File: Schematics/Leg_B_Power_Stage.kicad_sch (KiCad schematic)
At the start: 0 parts

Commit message: [LEG A WIP]
- moved circuits in Leg A HS and LS
- Completed 90% of HS and LS for LEG A
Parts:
- added Q5, Q6: C3M0025065K, SiC_Inverter:C3M0025065K, symbol SiC_Inverter:C3M0025065K
- added U3, U4: UCC21710QDWRQ1, SiC_Inverter:UCC21710QDWRQ1, symbol SiC_Inverter:UCC21710QDWRQ1

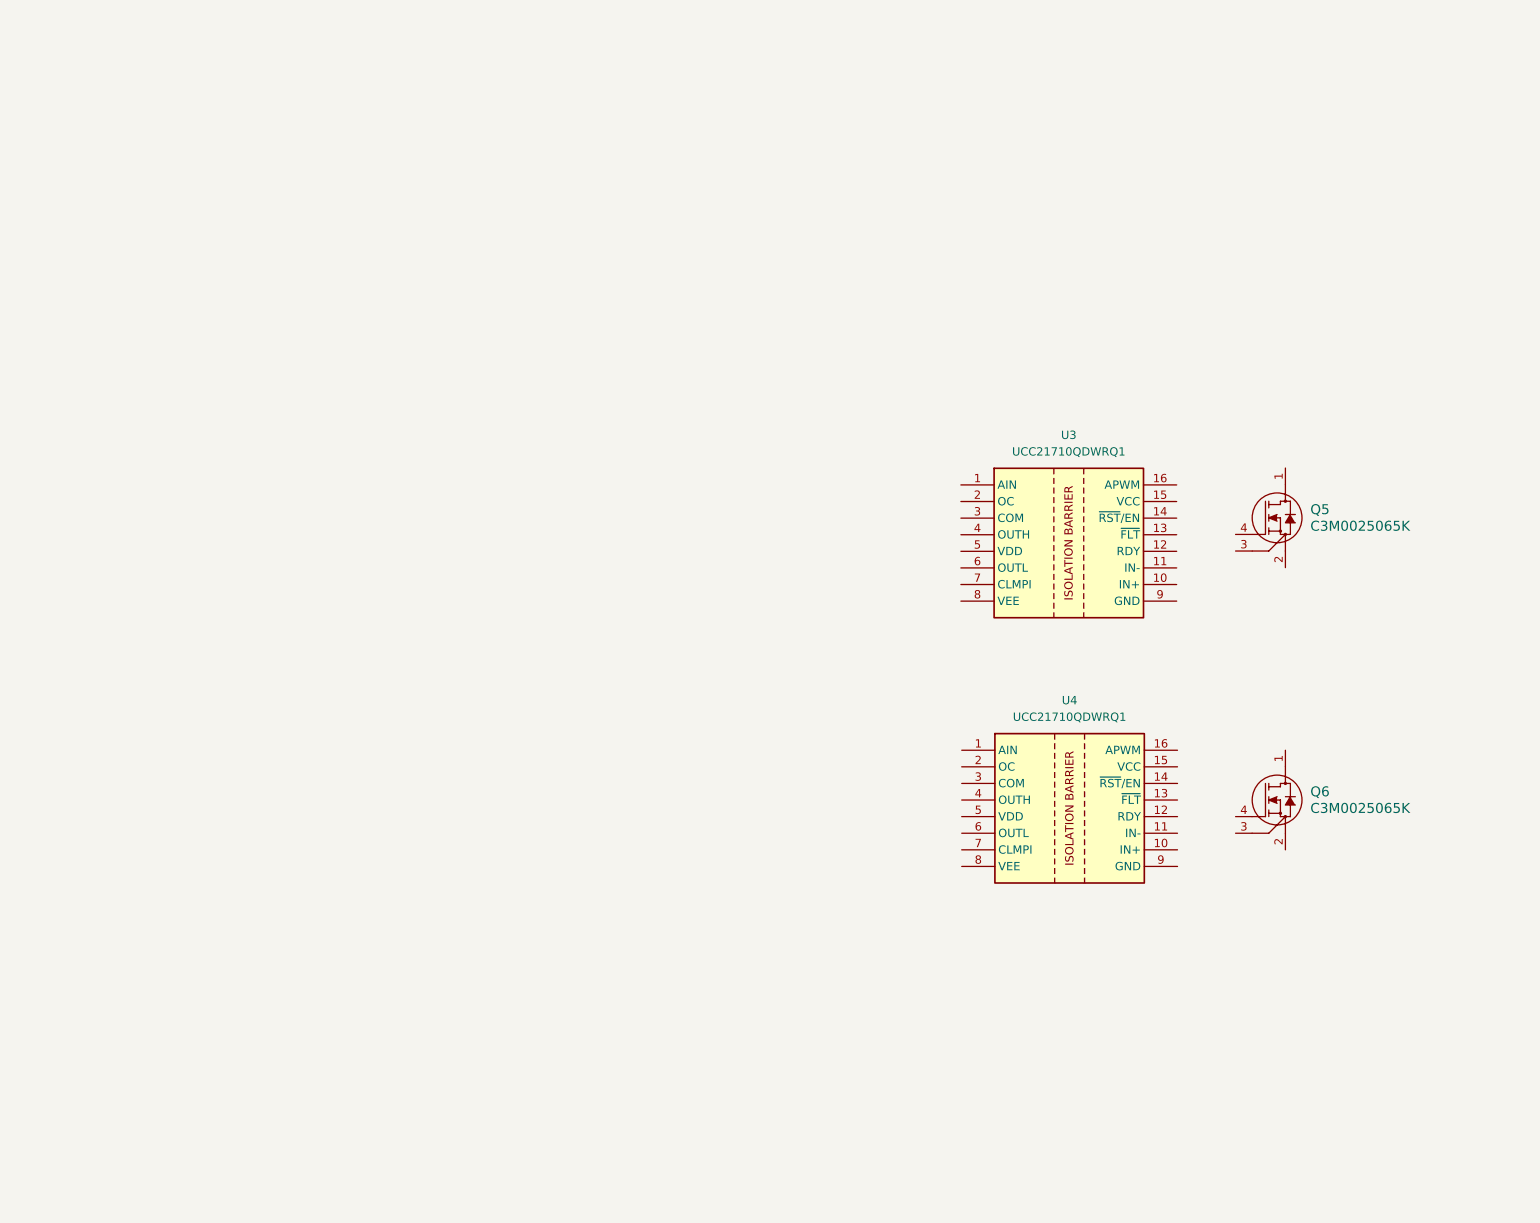
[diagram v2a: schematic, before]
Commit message: Copy past Leg A onto Leg B, Changed hames on both High/Low side to match Leg B
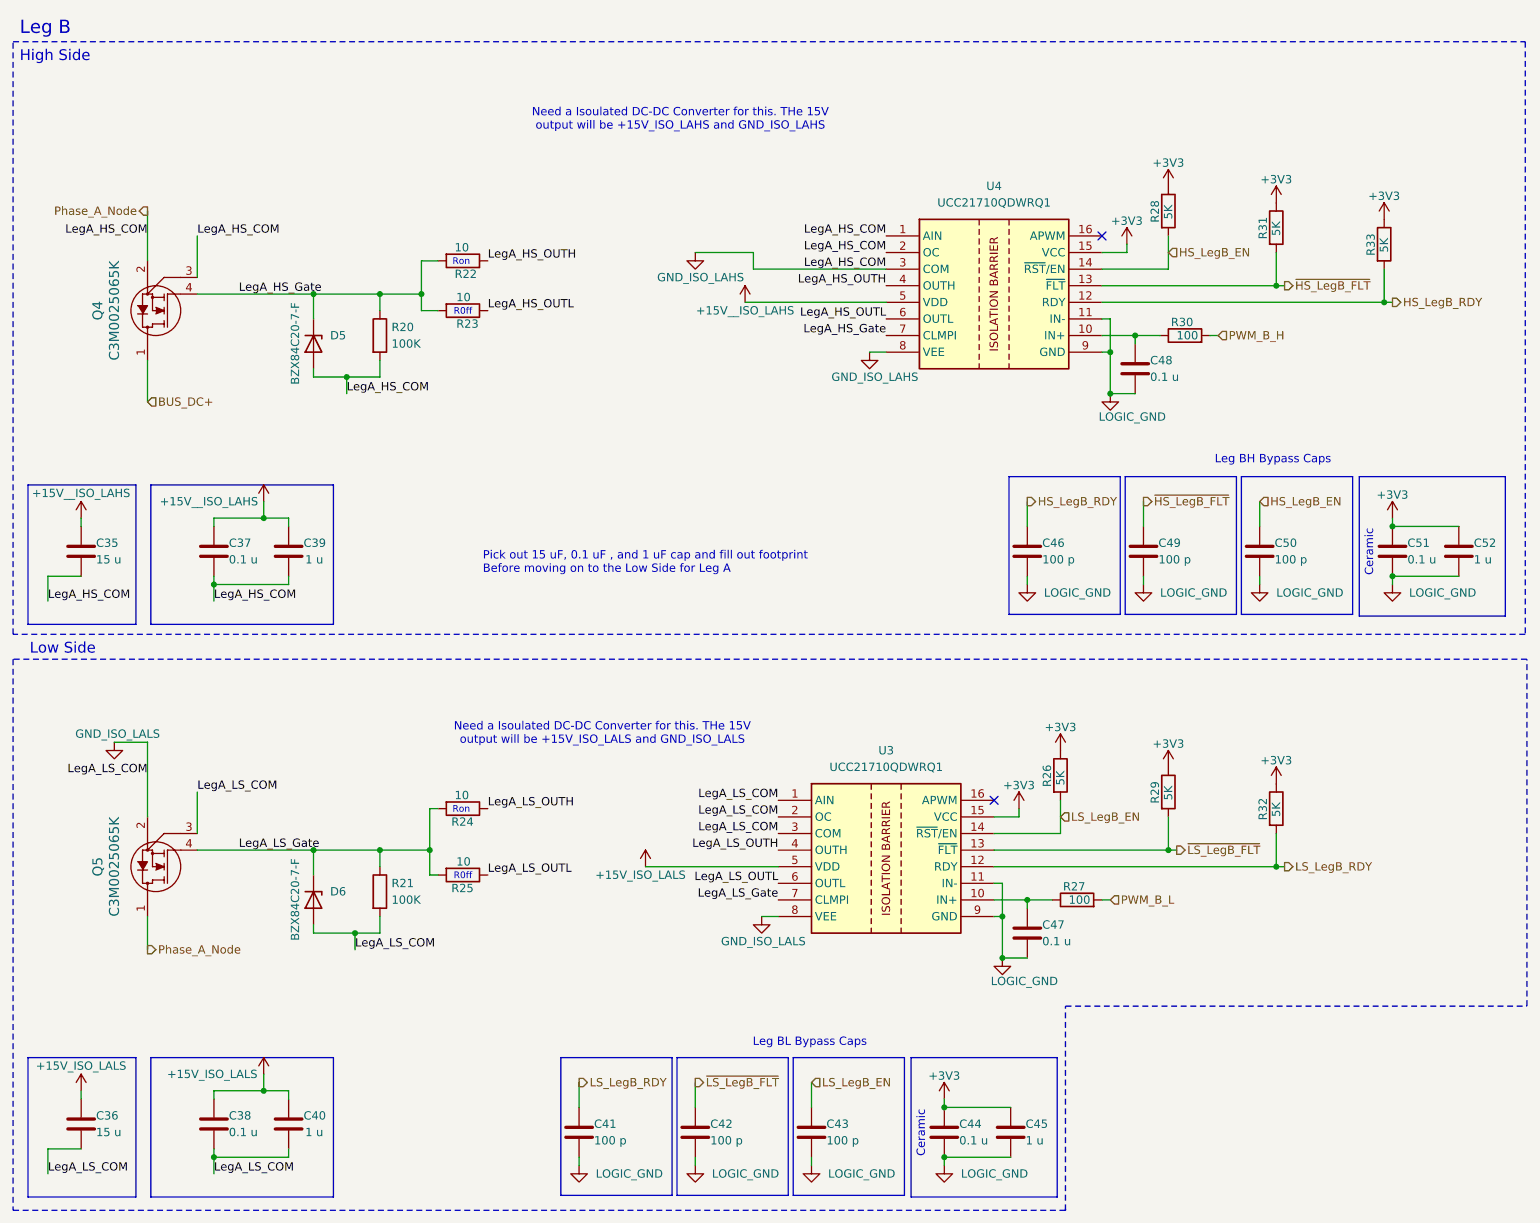
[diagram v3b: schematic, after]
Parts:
- removed Q6: C3M0025065K, SiC_Inverter:C3M0025065K, symbol SiC_Inverter:C3M0025065K
- added C35, C36: 15 u, symbol Device:C
- added C37, C38, C44, C47, C48, C51: 0.1 u, symbol Device:C
- added C39, C40, C45, C52: 1 u, symbol Device:C
- added C41, C42, C43, C46, C49, C50: 100 p, symbol Device:C
- added D5, D6: BZX84C20-7-F, Package_TO_SOT_SMD:SOT-23-3, symbol SiC_Inverter:BZX84C20-7-F
- added Q4: C3M0025065K, SiC_Inverter:C3M0025065K, symbol SiC_Inverter:C3M0025065K
- added R20, R21: 100K, Resistor_SMD:R_1206_3216Metric_Pad1.30x1.75mm_HandSolder, symbol Device:R
- added R22, R23, R24, R25: 10, Resistor_SMD:R_1206_3216Metric_Pad1.30x1.75mm_HandSolder, symbol Device:R
- added R26, R28, R29, R31, R32, R33: 5K, Resistor_SMD:R_1206_3216Metric_Pad1.30x1.75mm_HandSolder, symbol Device:R
- added R27, R30: 100, Resistor_SMD:R_1206_3216Metric_Pad1.30x1.75mm_HandSolder, symbol Device:R
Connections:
- net GND_ISO_LAHS: now reaches U4.1 (AIN)
- net GND_ISO_LAHS: now also Q5.1, U4.2 (OC), U4.3 (COM), U4.8 (VEE), C35.2, C37.2, C39.2, D5.2 (A), Q4.2, Q4.3, R20.2
- net at U4.10 (IN+): now also C48.1, R30.1
- net LOGIC_GND: now reaches U4.11 (IN-)
- net LOGIC_GND: now also U3.11 (IN-), U3.9 (GND), U4.9 (GND), C41.2, C42.2, C43.2, C44.2, C45.2, C46.2, C47.2, C48.2, C49.2, C50.2, C51.2, C52.2
- net HS_LegB_RDY: now reaches U4.12 (RDY)
- net HS_LegB_RDY: now also C46.1, R33.2
- net ~{HS_LegB_FLT}: now reaches U4.13 (~{FLT})
- net ~{HS_LegB_FLT}: now also C49.1, R31.2
- net HS_LegB_EN: now reaches U4.14 (~{RST}/EN)
- net HS_LegB_EN: now also C50.1, R28.2
- net +3V3: now reaches U4.15 (VCC)
- net +3V3: now also U3.15 (VCC), C44.1, C45.1, C51.1, C52.1, R26.1, R28.1, R29.1, R31.1, R32.1, R33.1
- net LegA_HS_OUTH: now reaches U4.4 (OUTH)
- net LegA_HS_OUTH: now also R22.1
- net +15V__ISO_LAHS: now reaches U4.5 (VDD)
- net +15V__ISO_LAHS: now also C35.1, C37.1, C39.1
- net LegA_HS_OUTL: now reaches U4.6 (OUTL)
- net LegA_HS_OUTL: now also R23.1
- net LegA_HS_Gate: now reaches U4.7 (CLMPI)
- net LegA_HS_Gate: now also D5.1 (K), Q4.4, R20.1, R22.2, R23.2
- net GND_ISO_LALS: now reaches U3.1 (AIN)
- net GND_ISO_LALS: now also Q5.2, Q5.3, U3.2 (OC), U3.3 (COM), U3.8 (VEE), C36.2, C38.2, C40.2, D6.2 (A), R21.2
- net at U3.10 (IN+): now also C47.1, R27.1
- net LS_LegB_RDY: now reaches U3.12 (RDY)
- net LS_LegB_RDY: now also C41.1, R32.2
- net ~{LS_LegB_FLT}: now reaches U3.13 (~{FLT})
- net ~{LS_LegB_FLT}: now also C42.1, R29.2
- net LS_LegB_EN: now reaches U3.14 (~{RST}/EN)
- net LS_LegB_EN: now also C43.1, R26.2
- net LegA_LS_OUTH: now reaches U3.4 (OUTH)
- net LegA_LS_OUTH: now also R24.1
- net +15V_ISO_LALS: now reaches U3.5 (VDD)
- net +15V_ISO_LALS: now also C36.1, C38.1, C40.1
- net LegA_LS_OUTL: now reaches U3.6 (OUTL)
- net LegA_LS_OUTL: now also R25.1
- net LegA_LS_Gate: now reaches U3.7 (CLMPI)
- net LegA_LS_Gate: now also Q5.4, D6.1 (K), R21.1, R24.2, R25.2
- new net BUS_DC+: Q4.1
- new net PWM_B_H: R30.2
- new net PWM_B_L: R27.2
- no-connect marks 0 -> 2
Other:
- note added: "Ceramic"
- note added: "High Side"
- note added: "Leg B"
- note added: "Leg BH Bypass Caps"
- note added: "Leg BL Bypass Caps"
- note added: "Low Side"
- note added: "Need a Isoulated DC-DC Converter for this. THe 15V output will be +15V_ISO_LAHS and GND_ISO_LAHS"
- note added: "Need a Isoulated DC-DC Converter for this. THe 15V output will be +15V_ISO_LALS and GND_ISO_LALS"
- note added: "Pick out 15 uF, 0.1 uF , and 1 uF cap and fill out footprint Before moving on to the Low Side for Leg A"
- note added: "R0ff"
- note added: "Ron"

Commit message: [WIP Full Bridge]
- Finished Leg B and cleaned up sub sheets Leg A and Leg B
- Added Hierarchical sheet pins for Leg A,B and Full Bridge
- Added power schamtic for future use
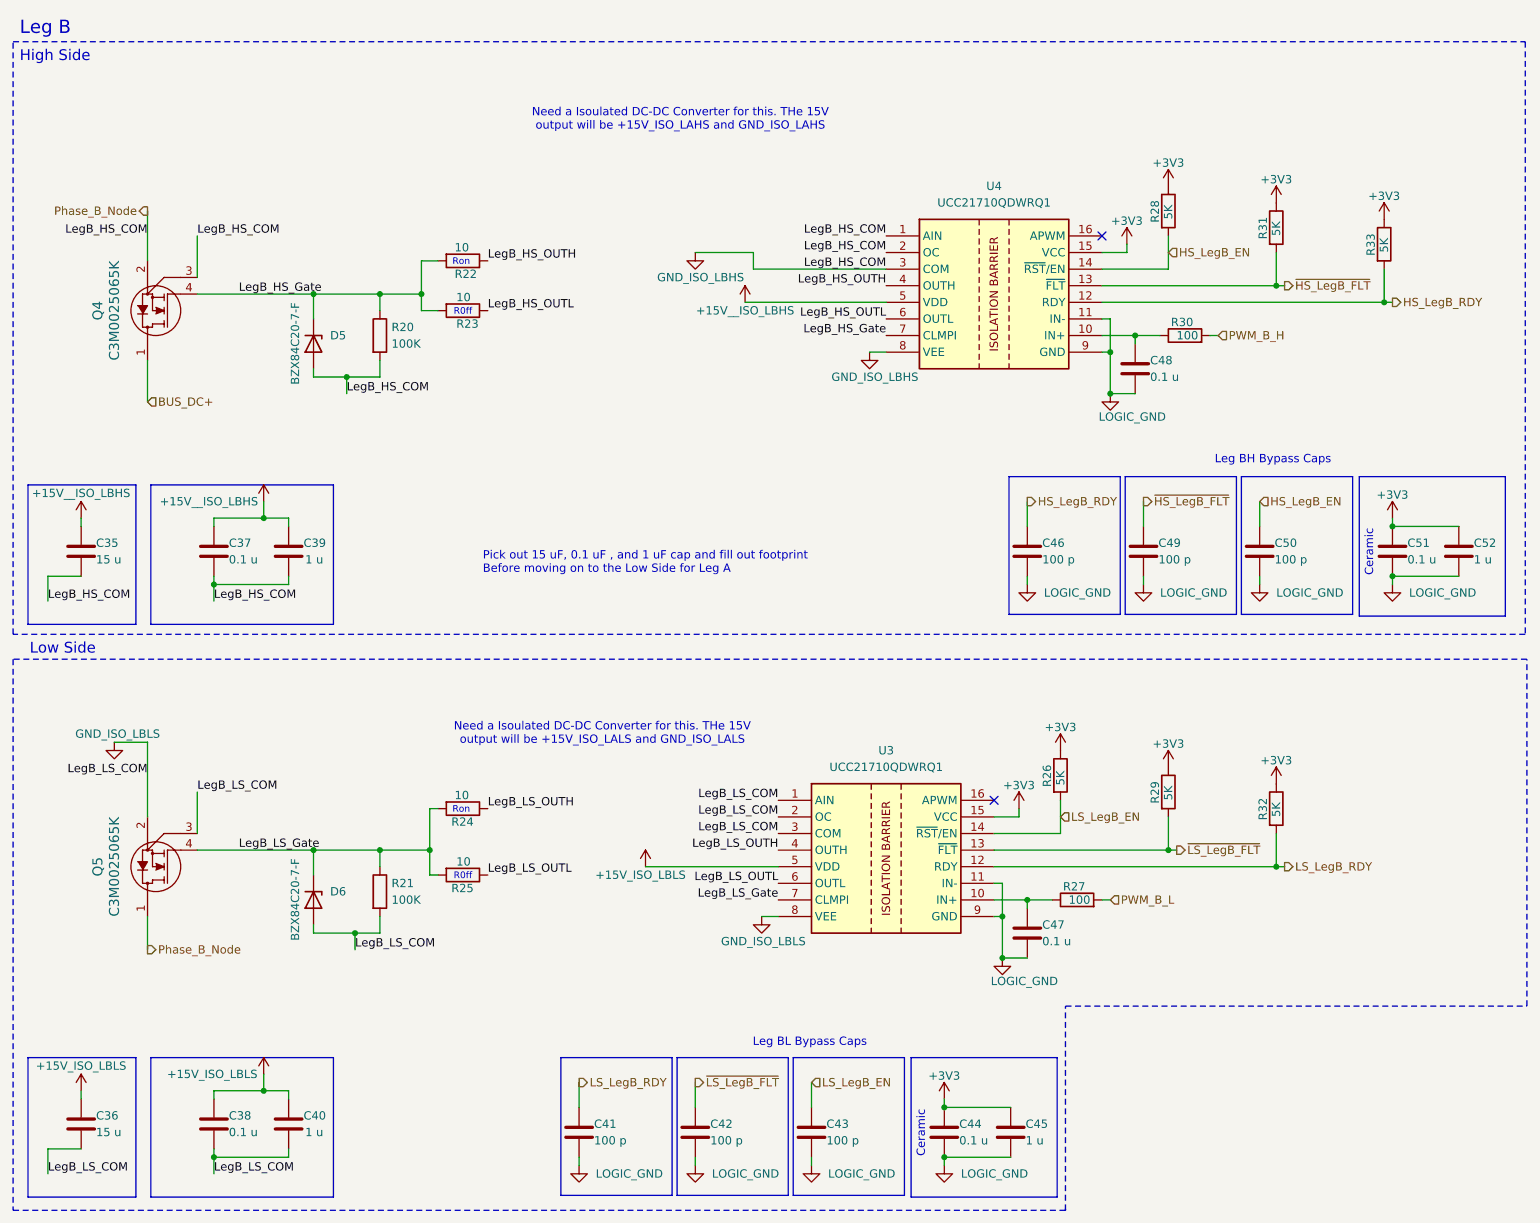
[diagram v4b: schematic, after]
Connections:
- net +15V_ISO_LALS renamed +15V_ISO_LBLS
- net +15V__ISO_LAHS renamed +15V__ISO_LBHS
- net GND_ISO_LAHS renamed GND_ISO_LBHS
- net GND_ISO_LALS renamed GND_ISO_LBLS
- net LegA_HS_Gate renamed LegB_HS_Gate
- net LegA_HS_OUTH renamed LegB_HS_OUTH
- net LegA_HS_OUTL renamed LegB_HS_OUTL
- net LegA_LS_Gate renamed LegB_LS_Gate
- net LegA_LS_OUTH renamed LegB_LS_OUTH
- net LegA_LS_OUTL renamed LegB_LS_OUTL

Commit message: Added Footprints for Cap size 15u, 1u, 0.1u and 100p
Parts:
- C35, C36: footprint (none) -> Capacitor_SMD:C_1206_3216Metric_Pad1.33x1.80mm_HandSolder; symbol Device:C -> SiC_Inverter:C3216X5R1E156M160AB
- C37, C38, C44, C47, C48, C51: footprint (none) -> Capacitor_SMD:C_0805_2012Metric_Pad1.18x1.45mm_HandSolder; symbol Device:C -> SiC_Inverter:C2012X8R1E105M125AE
- C39, C40, C45, C52: footprint (none) -> Capacitor_SMD:C_1206_3216Metric_Pad1.33x1.80mm_HandSolder; symbol Device:C -> SiC_Inverter:C3216X8R1E105M160AA
- C41, C42, C43, C46, C49, C50: footprint (none) -> Capacitor_SMD:C_0603_1608Metric_Pad1.08x0.95mm_HandSolder; symbol Device:C -> SiC_Inverter:CGA1A2X7R1C101K030BA
